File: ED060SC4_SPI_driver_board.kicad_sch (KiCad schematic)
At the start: 23 parts, among them J2 Conn_01x06, J3 Conn_01x04, J4 Conn_01x04, SW1 SW_SPDT, U2 STM32F103C8T6, Y1 16MHz, 10pF

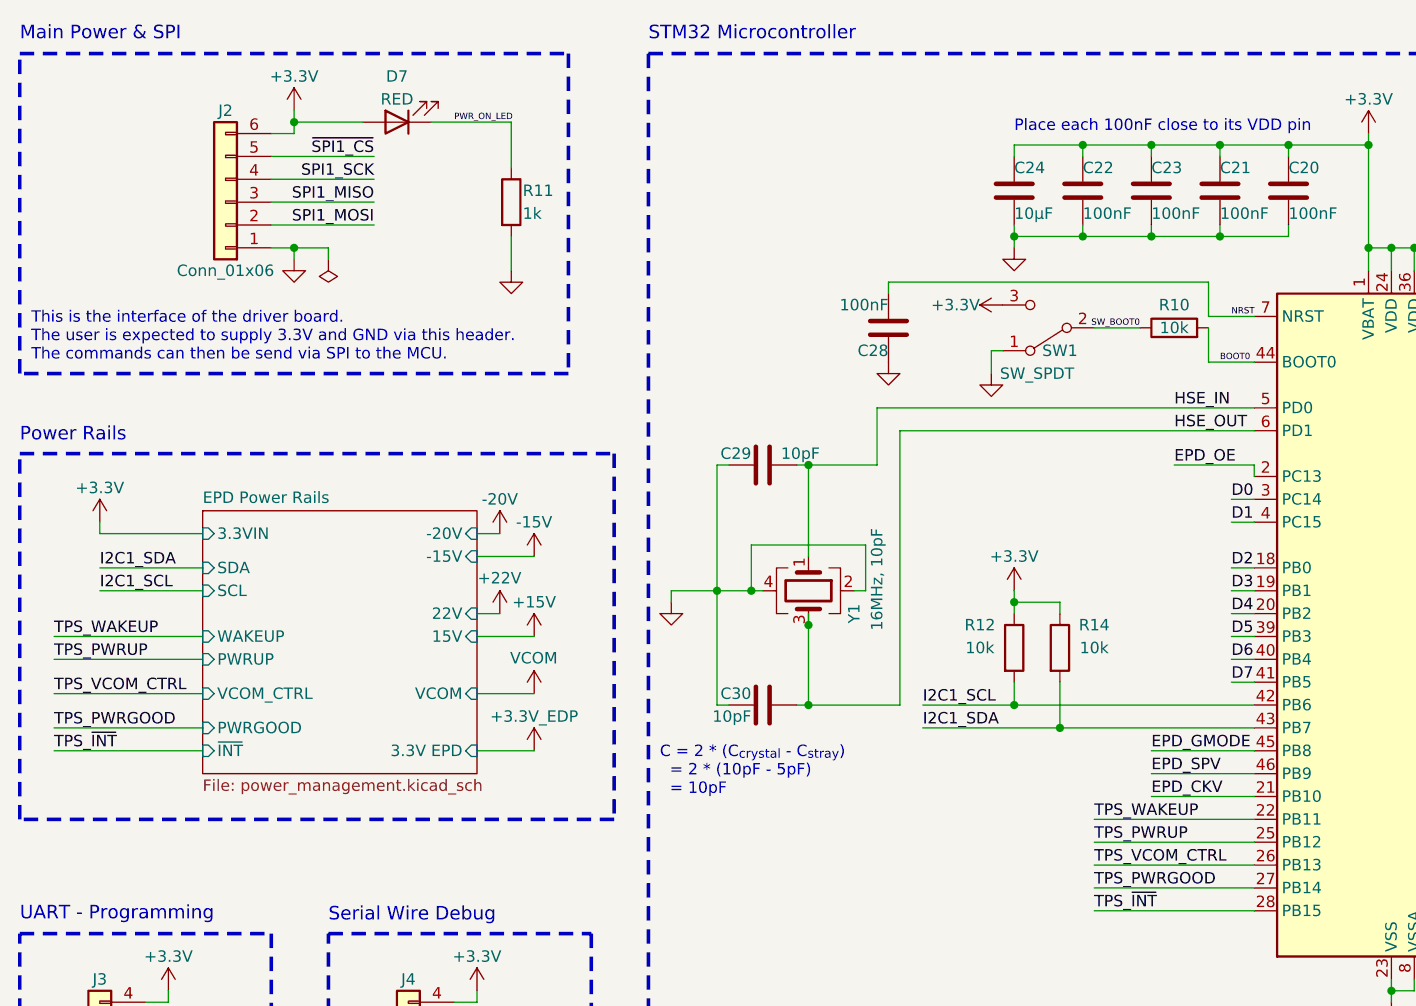
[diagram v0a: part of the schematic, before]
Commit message: Use DIP switch for power LED
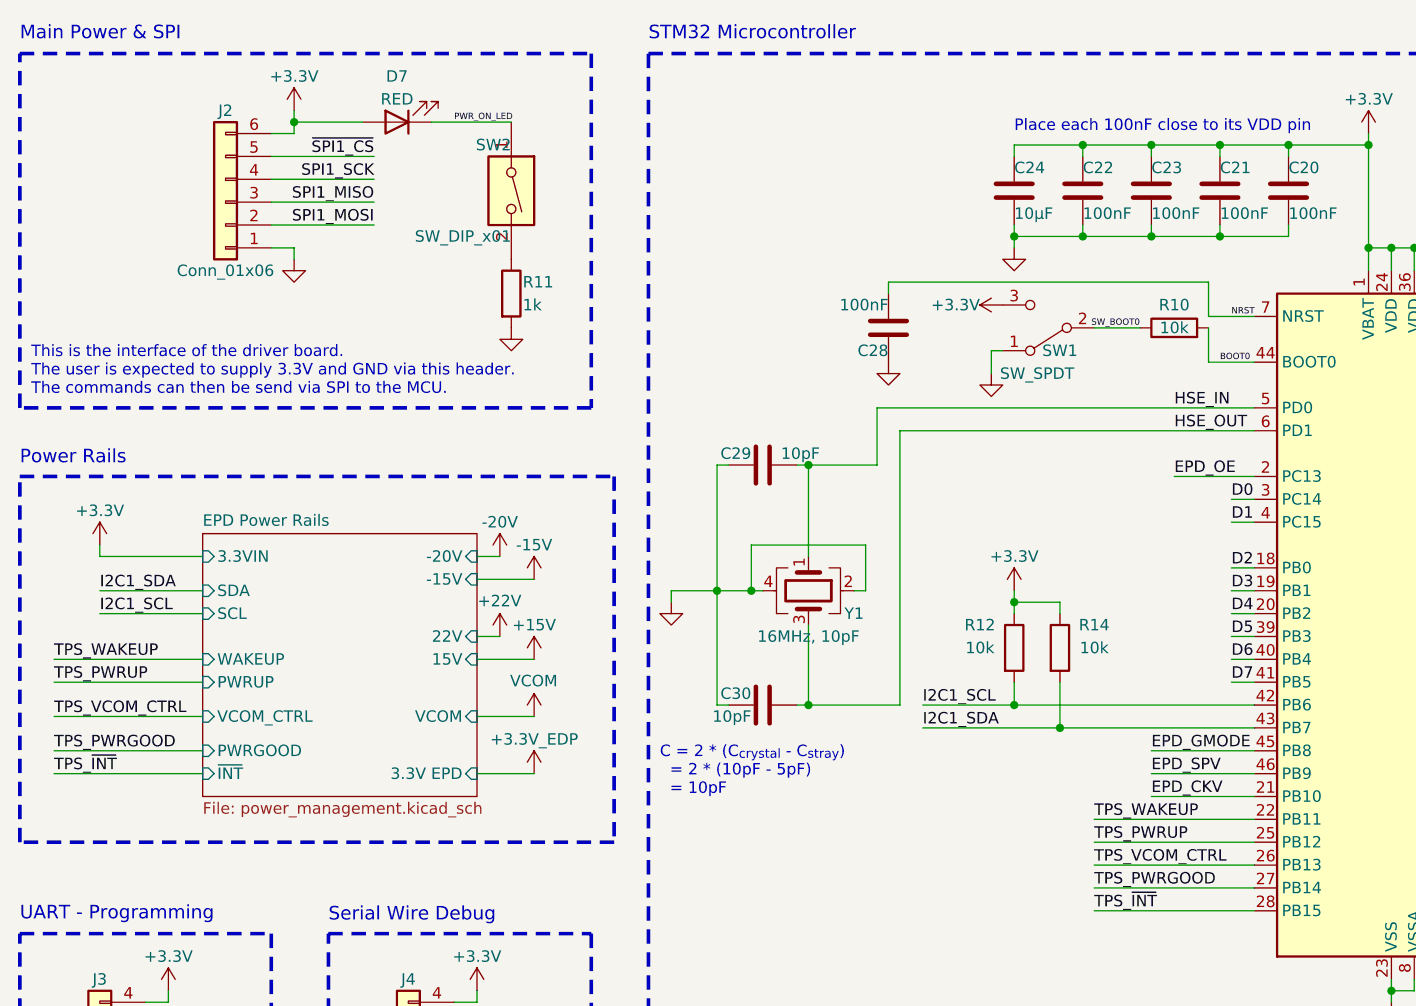
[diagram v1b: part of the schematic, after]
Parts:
- added SW2: SW_DIP_x01, symbol Switch:SW_DIP_x01
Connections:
- net PWR_ON_LED: now also SW2.1; no longer R11.1
- new net: R11.1, SW2.2
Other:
- moved on the sheet: R11

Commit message: Update library path and add DIP switch
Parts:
- SW2: footprint (none) -> local_lib:DSIC01LSGET
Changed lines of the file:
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@@
       (effects (font (size 1.27 1.27)) (justify right))
     )
-    (property "Footprint" "" (at 69.85 49.53 0)
+    (property "Footprint" "local_lib:DSIC01LSGET" (at 69.85 49.53 0)
       (effects (font (size 1.27 1.27)) hide)
     )
-    (property "Datasheet" "~" (at 69.85 49.53 0)
+    (property "Datasheet" "https://datasheet.lcsc.com/lcsc/1811041512_DongGuan-KINGTEK-Industrial-Co--LTD-DSIC01LSGET_C54948.pdf" (at 69.85 49.53 0)
       (effects (font (size 1.27 1.27)) hide)
     )

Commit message: set value of dip led switch
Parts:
- SW2: value SW_DIP_x01 -> DSIC01LSGET
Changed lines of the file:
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@@
       (effects (font (size 1.27 1.27)) (justify right))
     )
-    (property "Value" "SW_DIP_x01" (at 69.85 54.61 90)
+    (property "Value" "DSIC01LSGET" (at 69.85 54.61 90)
       (effects (font (size 1.27 1.27)) (justify right))
     )

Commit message: Add footprints and some labels
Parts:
- C20, C21, C22, C23, C24, C25, C26, C27, C28, C29, C30: footprint (none) -> Capacitor_SMD:C_0603_1608Metric
- D7: footprint (none) -> LED_SMD:LED_0603_1608Metric
- FB1, R10, R11, R12, R14: footprint (none) -> Resistor_SMD:R_0603_1608Metric
- J2: footprint (none) -> Connector_PinHeader_2.54mm:PinHeader_1x06_P2.54mm_Vertical
- J3, J4: footprint (none) -> Connector_PinSocket_2.54mm:PinSocket_1x04_P2.54mm_Vertical
- Y1: footprint (none) -> Crystal:Crystal_SMD_3225-4Pin_3.2x2.5mm
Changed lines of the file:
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@@
       (effects (font (size 1.27 1.27)))
     )
-    (property "Footprint" "" (at 58.42 144.78 0)
+    (property "Footprint" "Connector_PinSocket_2.54mm:PinSocket_1x04_P2.54mm_Vertical" (at 58.42 144.78 0)
       (effects (font (size 1.27 1.27)) hide)
     )
@@
       (effects (font (size 1.27 1.27)) (justify left))
     )
-    (property "Footprint" "" (at 126.6952 53.34 0)
+    (property "Footprint" "Capacitor_SMD:C_0603_1608Metric" (at 126.6952 53.34 0)
       (effects (font (size 1.27 1.27)) hide)
     )
@@
       (effects (font (size 1.27 1.27)))
     )
-    (property "Footprint" "" (at 200.66 46.228 90)
+    (property "Footprint" "Resistor_SMD:R_0603_1608Metric" (at 200.66 46.228 90)
       (effects (font (size 1.27 1.27)) hide)
     )
@@
       (effects (font (size 1.27 1.27)) (justify left))
     )
-    (property "Footprint" "" (at 211.7852 53.34 0)
+    (property "Footprint" "Capacitor_SMD:C_0603_1608Metric" (at 211.7852 53.34 0)
       (effects (font (size 1.27 1.27)) hide)
     )
@@
       (effects (font (size 1.27 1.27)) (justify left))
     )
-    (property "Footprint" "" (at 190.1952 53.34 0)
+    (property "Footprint" "Capacitor_SMD:C_0603_1608Metric" (at 190.1952 53.34 0)
       (effects (font (size 1.27 1.27)) hide)
     )
@@
       (effects (font (size 1.27 1.27)) (justify left))
     )
-    (property "Footprint" "" (at 157.1752 53.34 0)
+    (property "Footprint" "Capacitor_SMD:C_0603_1608Metric" (at 157.1752 53.34 0)
       (effects (font (size 1.27 1.27)) hide)
     )
@@
       (effects (font (size 1.27 1.27)) (justify left))
     )
-    (property "Footprint" "" (at 134.3152 53.34 0)
+    (property "Footprint" "Capacitor_SMD:C_0603_1608Metric" (at 134.3152 53.34 0)
       (effects (font (size 1.27 1.27)) hide)
     )
@@
       (effects (font (size 1.27 1.27)))
     )
-    (property "Footprint" "" (at 57.15 41.91 0)
+    (property "Footprint" "LED_SMD:LED_0603_1608Metric" (at 57.15 41.91 0)
       (effects (font (size 1.27 1.27)) hide)
     )
@@
       (effects (font (size 1.27 1.27)))
     )
-    (property "Footprint" "" (at 102.87 93.98 0)
+    (property "Footprint" "Crystal:Crystal_SMD_3225-4Pin_3.2x2.5mm" (at 102.87 93.98 0)
       (effects (font (size 1.27 1.27)) hide)
     )
@@
       (effects (font (size 1.27 1.27)) (justify left))
     )
-    (property "Footprint" "" (at 101.6 105.7148 0)
+    (property "Footprint" "Capacitor_SMD:C_0603_1608Metric" (at 101.6 105.7148 0)
       (effects (font (size 1.27 1.27)) hide)
     )
@@
       (effects (font (size 1.27 1.27)))
     )
-    (property "Footprint" "" (at 129.032 100.33 90)
+    (property "Footprint" "Resistor_SMD:R_0603_1608Metric" (at 129.032 100.33 90)
       (effects (font (size 1.27 1.27)) hide)
     )
@@
       (effects (font (size 1.27 1.27)) (justify left))
     )
-    (property "Footprint" "" (at 110.7948 60.96 0)
+    (property "Footprint" "Capacitor_SMD:C_0603_1608Metric" (at 110.7948 60.96 0)
       (effects (font (size 1.27 1.27)) hide)
     )
@@
       (effects (font (size 1.27 1.27)) (justify left))
     )
-    (property "Footprint" "" (at 68.072 60.96 90)
+    (property "Footprint" "Resistor_SMD:R_0603_1608Metric" (at 68.072 60.96 90)
       (effects (font (size 1.27 1.27)) hide)
     )
@@
       (effects (font (size 1.27 1.27)))
     )
-    (property "Footprint" "" (at 38.1 50.8 0)
+    (property "Footprint" "Connector_PinHeader_2.54mm:PinHeader_1x06_P2.54mm_Vertical" (at 38.1 50.8 0)
       (effects (font (size 1.27 1.27)) hide)
     )
@@
       (effects (font (size 1.27 1.27)))
     )
-    (property "Footprint" "" (at 24.13 144.78 0)
+    (property "Footprint" "Connector_PinSocket_2.54mm:PinSocket_1x04_P2.54mm_Vertical" (at 24.13 144.78 0)
       (effects (font (size 1.27 1.27)) hide)
     )
@@
       (effects (font (size 1.27 1.27)) (justify left))
     )
-    (property "Footprint" "" (at 101.6 79.0448 0)
+    (property "Footprint" "Capacitor_SMD:C_0603_1608Metric" (at 101.6 79.0448 0)
       (effects (font (size 1.27 1.27)) hide)
     )
@@
       (effects (font (size 1.27 1.27)))
     )
-    (property "Footprint" "" (at 143.51 66.548 90)
+    (property "Footprint" "Resistor_SMD:R_0603_1608Metric" (at 143.51 66.548 90)
       (effects (font (size 1.27 1.27)) hide)
     )
@@
       (effects (font (size 1.27 1.27)) (justify left))
     )
-    (property "Footprint" "" (at 181.3052 53.34 0)
+    (property "Footprint" "Capacitor_SMD:C_0603_1608Metric" (at 181.3052 53.34 0)
       (effects (font (size 1.27 1.27)) hide)
     )
@@
       (effects (font (size 1.27 1.27)) (justify left))
     )
-    (property "Footprint" "" (at 141.9352 53.34 0)
+    (property "Footprint" "Capacitor_SMD:C_0603_1608Metric" (at 141.9352 53.34 0)
       (effects (font (size 1.27 1.27)) hide)
     )
@@
       (effects (font (size 1.27 1.27)) (justify left))
     )
-    (property "Footprint" "" (at 149.5552 53.34 0)
+    (property "Footprint" "Capacitor_SMD:C_0603_1608Metric" (at 149.5552 53.34 0)
       (effects (font (size 1.27 1.27)) hide)
     )
@@
       (effects (font (size 1.27 1.27)))
     )
-    (property "Footprint" "" (at 123.952 100.33 90)
-      (effects (font (size 1.27 1.27)) hide)
-    )
+    (property "Footprint" "Resistor_SMD:R_0603_1608Metric" (at 123.952 100.33 90)
+      (effects (font (size 1.27 1.27)) hide)
+    )

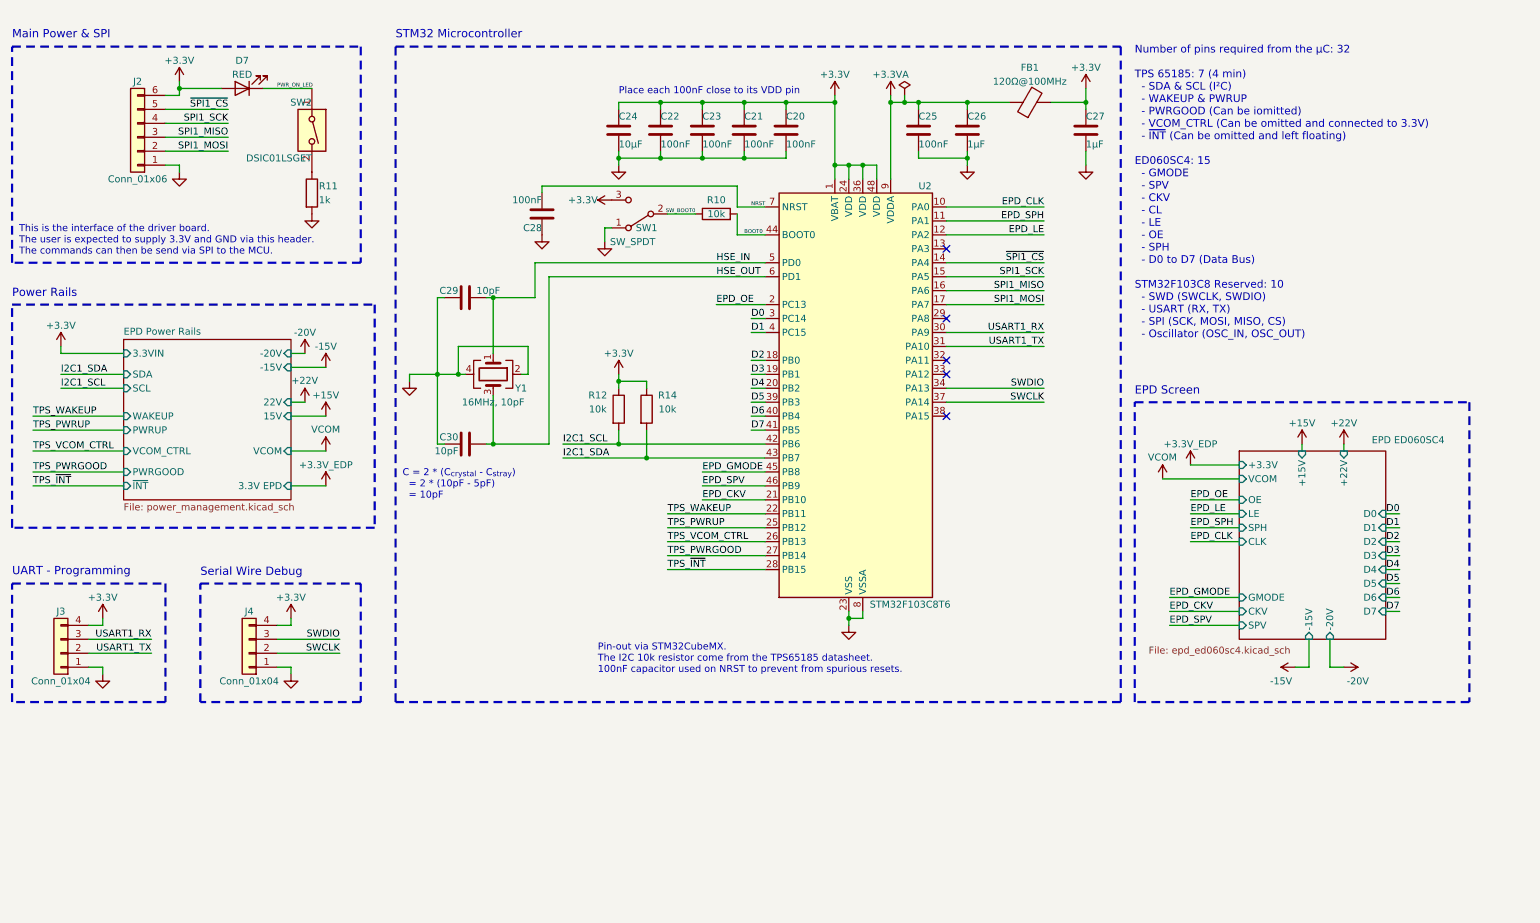
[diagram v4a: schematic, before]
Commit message: Add ESD and SPDT switch
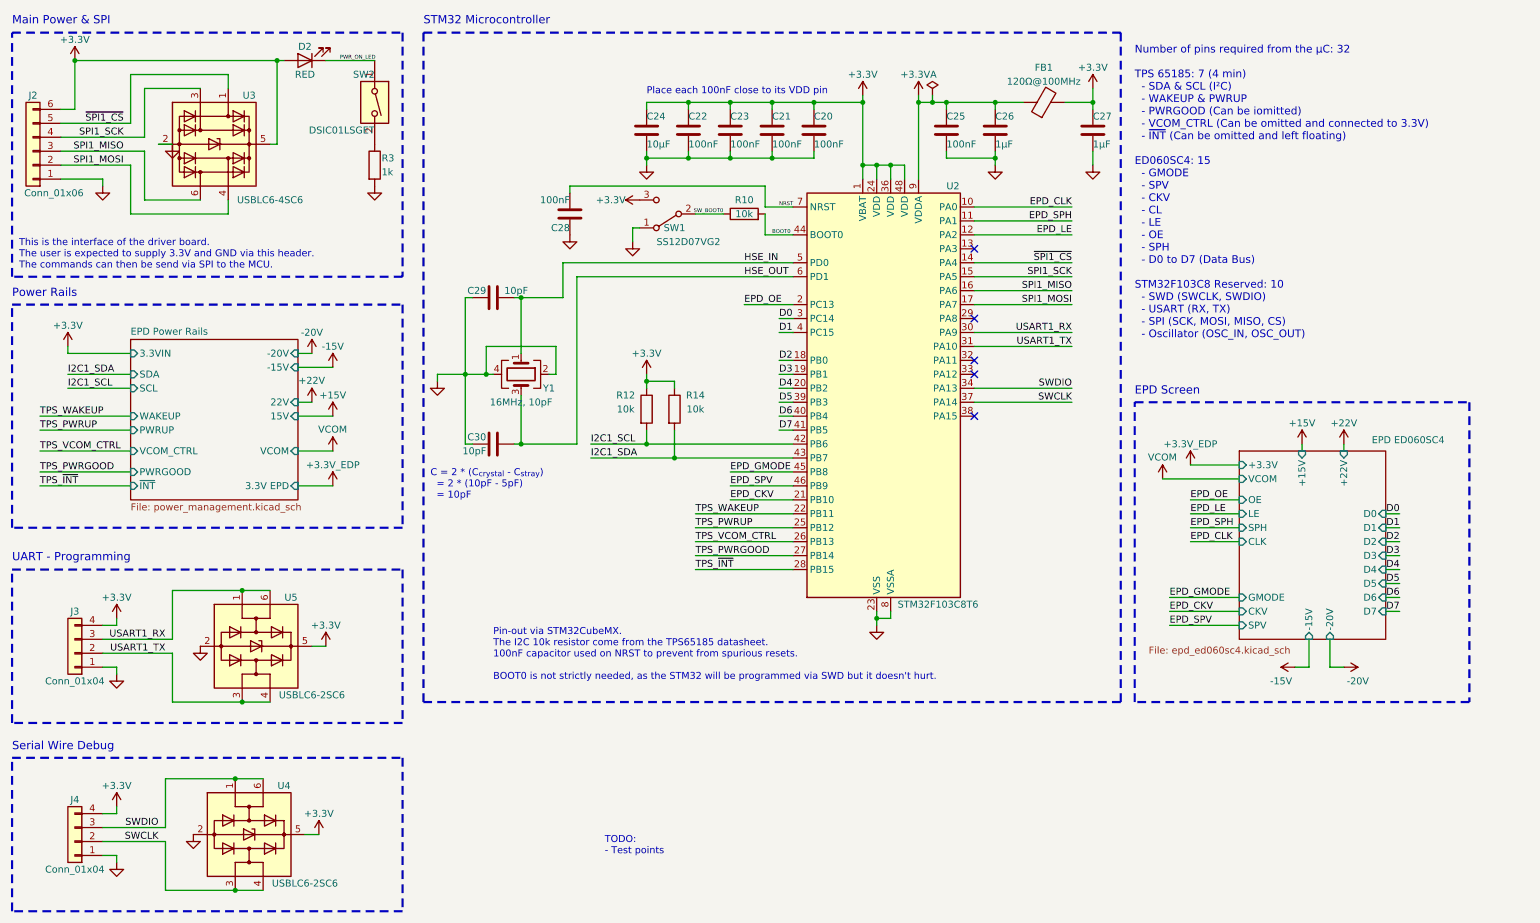
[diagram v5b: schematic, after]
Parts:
- removed D7: RED, LED_SMD:LED_0603_1608Metric, symbol Device:LED
- removed R11: 1k, Resistor_SMD:R_0603_1608Metric, symbol Device:R
- added D2: RED, LED_SMD:LED_0603_1608Metric, symbol Device:LED
- added R3: 1k, Resistor_SMD:R_0603_1608Metric, symbol Device:R
- added U3: USBLC6-4SC6, Package_TO_SOT_SMD:SOT-23-6, symbol Power_Protection:USBLC6-4SC6
- added U4, U5: USBLC6-2SC6, Package_TO_SOT_SMD:SOT-23-6, symbol Power_Protection:USBLC6-2SC6
- SW1: value SW_SPDT -> SS12D07VG2; footprint (none) -> local_lib:SW_SS12D07VG4
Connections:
- net +3.3V: now also D2.2 (A), U3.5 (VBUS), U4.5 (VBUS), U5.5 (VBUS)
- net GND: now also R3.2, U3.2 (GND), U4.2 (GND), U5.2 (GND)
- net PWR_ON_LED: now also D2.1 (K)
- net SPI1_MISO: now also U3.6 (I/O4)
- net SPI1_MOSI: now also U3.4 (I/O3)
- net SPI1_SCK: now also U3.3 (I/O2)
- net SWCLK: now also U4.3 (I/O2), U4.4 (I/O2)
- net SWDIO: now also U4.1 (I/O1), U4.6 (I/O1)
- net USART1_RX: now also U5.1 (I/O1), U5.6 (I/O1)
- net USART1_TX: now also U5.3 (I/O2), U5.4 (I/O2)
- net ~{SPI1_CS}: now also U3.1 (I/O1)
- net at SW2.2: now also R3.1
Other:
- note added: "Pin-out via STM32CubeMX. The I2C 10k resistor come from the TPS65185 datasheet. 100nF capacitor used on NRST to prevent from spurious resets. BOOT0 is not strictly needed, as the STM32 will be programmed via SWD but it doesn't hurt."
- note added: "TODO: - Test points"
- note removed: "Pin-out via STM32CubeMX. The I2C 10k resistor come from the TPS65185 datasheet. 100nF capacitor used on NRST to prevent from spurious resets."
- moved on the sheet: C20, C21, C22, C23, C24, C25, C26, C27, C28, C29, C30, FB1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
